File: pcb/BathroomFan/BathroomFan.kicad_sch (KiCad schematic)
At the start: 8 parts, among them U1 ESP32-DEVKIT-V1, U2 DHT11

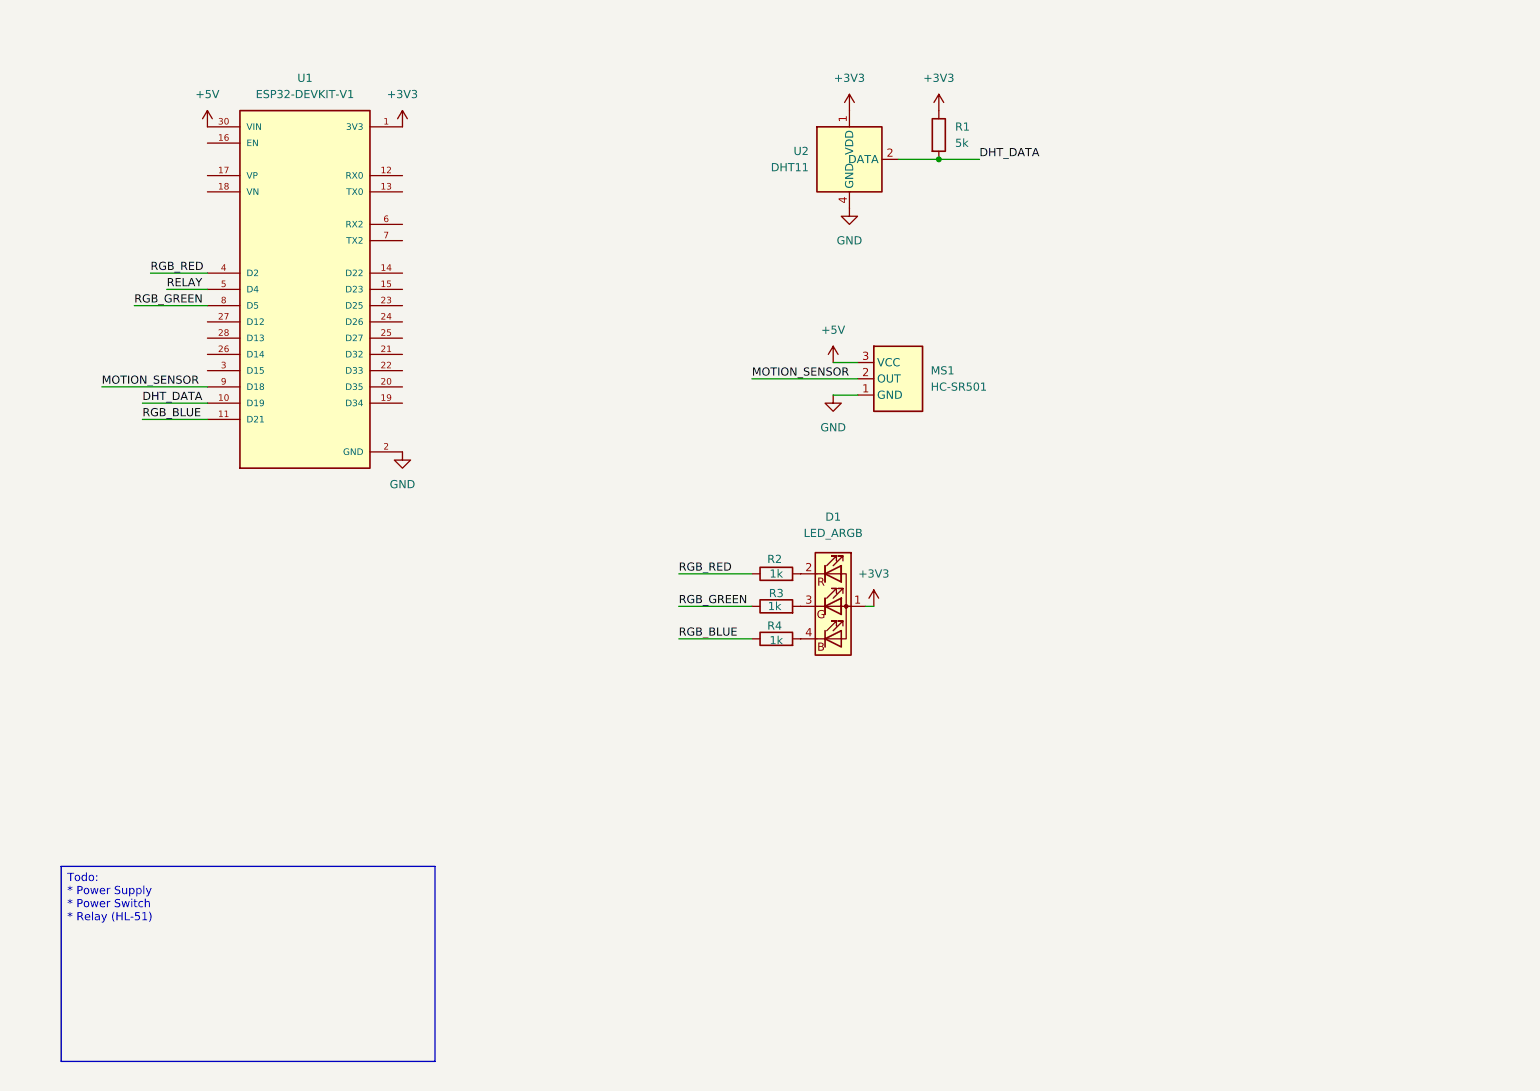
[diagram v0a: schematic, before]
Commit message: SCH - added ac/dc module with switch, relay and connectors for power and fan
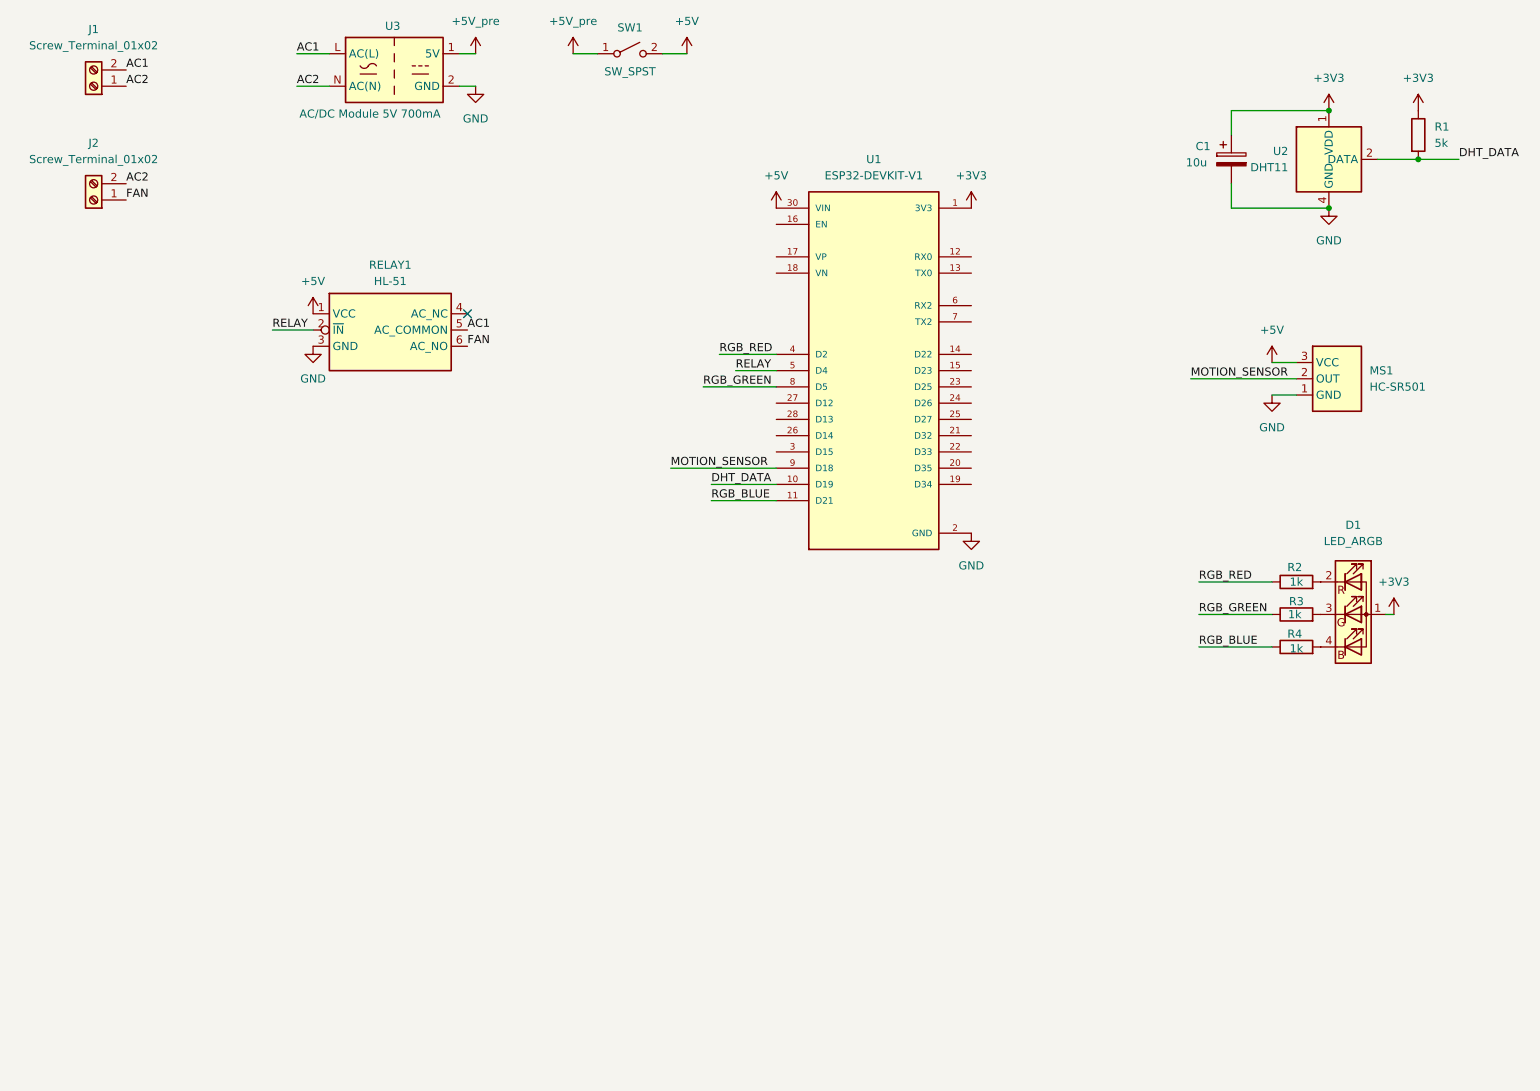
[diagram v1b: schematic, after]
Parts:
- added C1: 10u, symbol Device:C_Polarized
- added J1, J2: Screw_Terminal_01x02, symbol Connector:Screw_Terminal_01x02
- added RELAY1: HL-51, bathroom_fan:HL-51, symbol bathroom_fan:HL-51
- added SW1: SW_SPST, symbol Switch:SW_SPST
- added U3: AC/DC Module 5V 700mA, symbol bathroom_fan:AC-DC Module 5Vdc 700mA 85-265Vac
- D1: footprint (none) -> Connector_PinHeader_1.00mm:PinHeader_1x04_P1.00mm_Vertical
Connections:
- net +3V3: now also C1.1
- net +5V: now also RELAY1.1 (VCC), SW1.2 (B)
- net GND: now also C1.2, RELAY1.3 (GND), U3.2 (GND)
- net RELAY: now also RELAY1.2 (~{IN})
- new net +5V_pre: SW1.1 (A), U3.1 (5V)
- new net AC1: J1.2 (Pin_2), RELAY1.5 (AC_COMMON), U3.L (AC(L))
- new net AC2: J1.1 (Pin_1), J2.2 (Pin_2), U3.N (AC(N))
- new net FAN: J2.1 (Pin_1), RELAY1.6 (AC_NO)
- no-connect marks 0 -> 1
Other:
- moved on the sheet: D1, MS1, R1, R2, R3, R4, U1, U2

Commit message: improved relay footprint with actual part, added munting holes for screws
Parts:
- added H1, H2: MountingScrew, MountingHole:MountingHole_4.3mm_M4, symbol Auxiliary_Items:MountingScrew
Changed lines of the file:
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@@
+	)
+	(symbol
+		(lib_id "Auxiliary_Items:MountingScrew")
+		(at 137.16 179.07 0)
+		(unit 1)
+		(body_style 1)
+		(exclude_from_sim no)
+		(in_bom no)
+		(on_board yes)
+		(in_pos_files yes)
+		(dnp no)
+		(fields_autoplaced yes)
+		(property "Reference" "H2"
+			(at 137.16 175.006 0)
+			(hide yes)
+			(show_name no)
+			(do_not_autoplace no)
+			(effects
+				(font
+					(size 1.27 1.27)
+				)
+			)
+		)
+		(property "Value" "MountingScrew"
+			(at 137.16 182.626 0)
+			(hide yes)
+			(show_name no)
+			(do_not_autoplace no)
+			(effects
+				(font
+					(size 1.27 1.27)
+				)
+			)
+		)
+		(property "Footprint" "MountingHole:MountingHole_4.3mm_M4"
+			(at 137.16 179.07 0)
+			(hide yes)
+			(show_name no)
+			(do_not_autoplace no)
+			(effects
+				(font
+					(size 1.27 1.27)
+				)
+			)
+		)
+		(property "Datasheet" ""
+			(at 137.16 179.07 0)
+			(hide yes)
+			(show_name no)
+			(do_not_autoplace no)
+			(effects
+				(font
+					(size 1.27 1.27)
+				)
+			)
+		)
+		(property "Description" "Mounting screw"
+			(at 137.16 179.07 0)
+			(hide yes)
+			(show_name no)
+			(do_not_autoplace no)
+			(effects
+				(font
+					(size 1.27 1.27)
+				)
+			)
+		)
+		(instances
+			(project "BathroomFan"
+				(path "/4793d324-38ac-415b-8f0e-f54c1c7495b4"
+					(reference "H2")
+					(unit 1)
+				)
+			)
+		)
 	)
 	(symbol
@@
 					(unit 1)
 				)
+			)
+		)
+	)
+	(symbol
+		(lib_id "Auxiliary_Items:MountingScrew")
+		(at 132.08 179.07 0)
+		(unit 1)
+		(body_style 1)
+		(exclude_from_sim no)
+		(in_bom no)
+		(on_board yes)
+		(in_pos_files yes)
+		(dnp no)
+		(fields_autoplaced yes)
+		(property "Reference" "H1"
+			(at 132.08 175.006 0)
+			(hide yes)
+			(show_name no)
+			(do_not_autoplace no)
+			(effects
+				(font
+					(size 1.27 1.27)
+				)
+			)
+		)
+		(property "Value" "MountingScrew"
+			(at 132.08 182.626 0)
+			(hide yes)
+			(show_name no)
+			(do_not_autoplace no)
+			(effects
+				(font
+					(size 1.27 1.27)
+				)
+			)
+		)
+		(property "Footprint" "MountingHole:MountingHole_4.3mm_M4"
+			(at 132.08 179.07 0)
+			(hide yes)
+			(show_name no)
+			(do_not_autoplace no)
+			(effects
+				(font
+					(size 1.27 1.27)
+				)
+			)
+		)
+		(property "Datasheet" ""
+			(at 132.08 179.07 0)
+			(hide yes)
+			(show_name no)
+			(do_not_autoplace no)
+			(effects
+				(font
+					(size 1.27 1.27)
+				)
+			)
+		)
+		(property "Description" "Mounting screw"
+			(at 132.08 179.07 0)
+			(hide yes)
+			(show_name no)
+			(do_not_autoplace no)
+			(effects
+				(font
+					(size 1.27 1.27)
+				)
+			)
+		)
+		(instances
+			(project "BathroomFan"
+				(path "/4793d324-38ac-415b-8f0e-f54c1c7495b4"
+					(reference "H1")
+					(unit 1)
+				)

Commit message: PCB: initial Board format and component placement
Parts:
- C1: footprint (none) -> Capacitor_THT:CP_Radial_D4.0mm_P2.00mm
- D1: footprint Connector_PinHeader_1.00mm:PinHeader_1x04_P1.00mm_Vertical -> Connector_PinHeader_2.54mm:PinHeader_1x04_P2.54mm_Vertical
- J1: footprint (none) -> TerminalBlock_Phoenix:TerminalBlock_Phoenix_MKDS-1,5-2-5.08_1x02_P5.08mm_Horizontal; Name (none) -> POWER
- J2: footprint (none) -> TerminalBlock_Phoenix:TerminalBlock_Phoenix_MKDS-1,5-2-5.08_1x02_P5.08mm_Horizontal; Name (none) -> FAN
- MS1: footprint bathroom_fan:HC-SR501 -> Connector_PinHeader_2.54mm:PinHeader_1x03_P2.54mm_Vertical
- R1, R2, R3, R4: footprint (none) -> Resistor_SMD:R_0805_2012Metric_Pad1.20x1.40mm_HandSolder
- SW1: footprint (none) -> Connector_PinHeader_2.54mm:PinHeader_1x02_P2.54mm_Vertical
- U2: footprint Sensor:Aosong_DHT11_5.5x12.0_P2.54mm -> Connector_PinHeader_2.54mm:PinHeader_1x04_P2.54mm_Vertical
- U3: footprint (none) -> bathroom_fan:ACDC_Module_5V_700mA
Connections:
- net AC1: now also U3.N (AC(N)); no longer U3.L (AC(L))
- net AC2: now also U3.L (AC(L)); no longer U3.N (AC(N))
- net GND: now also U3.3 (GND); no longer U3.2 (GND)

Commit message: SCH and PCB: redistributed ESP32 pins for better layout, first version of layout finished
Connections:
- net MOTION_SENSOR: now also U1.28 (D13); no longer U1.9 (D18)
- net RELAY: now also U1.26 (D14); no longer U1.5 (D4)
- net RGB_BLUE: now also U1.5 (D4); no longer U1.11 (D21)
- net RGB_GREEN: now also U1.4 (D2); no longer U1.8 (D5)
- net RGB_RED: now also U1.3 (D15); no longer U1.4 (D2)
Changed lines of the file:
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@@
-	(wire
-		(pts
-			(xy 123.19 83.82) (xy 134.62 83.82)
-		)
-		(stroke
-			(width 0)
-			(type default)
-		)
-	)
 	(wire
 		(pts
@@
 	(wire
 		(pts
+			(xy 124.46 81.28) (xy 134.62 81.28)
+		)
+		(stroke
+			(width 0)
+			(type default)
+		)
+	)
+	(wire
+		(pts
 			(xy 205.74 52.07) (xy 205.74 55.88)
 		)
@@
 	(wire
 		(pts
-			(xy 124.46 101.6) (xy 134.62 101.6)
-		)
-		(stroke
-			(width 0)
-			(type default)
-		)
-	)
-	(wire
-		(pts
-			(xy 128.27 81.28) (xy 134.62 81.28)
-		)
-		(stroke
-			(width 0)
-			(type default)
-		)
-	)
-	(wire
-		(pts
 			(xy 85.09 36.83) (xy 87.63 36.83)
 		)
@@
 	(wire
 		(pts
+			(xy 123.19 78.74) (xy 134.62 78.74)
+		)
+		(stroke
+			(width 0)
+			(type default)
+		)
+	)
+	(wire
+		(pts
 			(xy 205.74 44.45) (xy 205.74 40.64)
 		)
@@
 	(wire
 		(pts
+			(xy 128.27 91.44) (xy 134.62 91.44)
+		)
+		(stroke
+			(width 0)
+			(type default)
+		)
+	)
+	(wire
+		(pts
 			(xy 124.46 99.06) (xy 134.62 99.06)
 		)
@@
 	(wire
 		(pts
-			(xy 125.73 78.74) (xy 134.62 78.74)
+			(xy 118.11 88.9) (xy 134.62 88.9)
 		)
 		(stroke
@@
 	(wire
 		(pts
+			(xy 125.73 93.98) (xy 134.62 93.98)
+		)
+		(stroke
+			(width 0)
+			(type default)
+		)
+	)
+	(wire
+		(pts
 			(xy 205.74 40.64) (xy 220.98 40.64)
 		)
@@
 		)
 	)
-	(wire
-		(pts
-			(xy 118.11 96.52) (xy 134.62 96.52)
-		)
-		(stroke
-			(width 0)
-			(type default)
+	(label "MOTION_SENSOR"
+		(at 118.11 88.9 0)
+		(effects
+			(font
+				(size 1.27 1.27)
+			)
+			(justify left bottom)
 		)
 	)
@@
 		)
 	)
-	(label "RGB_BLUE"
-		(at 124.46 101.6 0)
-		(effects
-			(font
-				(size 1.27 1.27)
-			)
-			(justify left bottom)
-		)
-	)
 	(label "AC1"
 		(at 86.36 74.93 0)
@@
 	)
 	(label "RGB_GREEN"
-		(at 123.19 83.82 0)
+		(at 123.19 78.74 0)
+		(effects
+			(font
+				(size 1.27 1.27)
+			)
+			(justify left bottom)
+		)
+	)
+	(label "RGB_RED"
+		(at 125.73 93.98 0)
 		(effects
 			(font
@@
 		)
 	)
+	(label "RGB_BLUE"
+		(at 124.46 81.28 0)
+		(effects
+			(font
+				(size 1.27 1.27)
+			)
+			(justify left bottom)
+		)
+	)
+	(label "RELAY"
+		(at 128.27 91.44 0)
+		(effects
+			(font
+				(size 1.27 1.27)
+			)
+			(justify left bottom)
+		)
+	)
 	(label "FAN"
 		(at 33.02 54.61 0)
@@
 	)
 	(label "RGB_RED"
-		(at 125.73 78.74 0)
-		(effects
-			(font
-				(size 1.27 1.27)
-			)
-			(justify left bottom)
-		)
-	)
-	(label "RGB_RED"
 		(at 200.66 114.3 0)
 		(effects
@@
 		)
 	)
-	(label "RELAY"
-		(at 128.27 81.28 0)
-		(effects
-			(font
-				(size 1.27 1.27)
-			)
-			(justify left bottom)
-		)
-	)
 	(label "AC1"
 		(at 33.02 34.29 0)
@@
 		(effects
 			(font
-				(size 1.27 1.27)
-			)
-			(justify left bottom)
-		)
-	)
-	(label "MOTION_SENSOR"
-		(at 118.11 96.52 0)
-		(effects
-			(font

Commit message: SCH and PCB: added logo, adjusted silk identifier
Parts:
- added G1: LOGO, bathroom_fan:LOGO, symbol bathroom_fan:LOGO
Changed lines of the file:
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@@
 	(title_block
 		(title "Bathroom Fan Controller")
-		(date "2026-07-05")
+		(date "2026-08-02")
 		(rev "1.0")
 		(company "brunolalb@gmail.com")
@@
 					(unit 1)
 				)
+			)
+		)
+	)
+	(symbol
+		(lib_id "bathroom_fan:LOGO")
+		(at 134.62 187.96 0)
+		(unit 1)
+		(body_style 1)
+		(exclude_from_sim no)
+		(in_bom no)
+		(on_board yes)
+		(in_pos_files yes)
+		(dnp no)
+		(fields_autoplaced yes)
+		(property "Reference" "G1"
+			(at 134.62 183.5948 0)
+			(hide yes)
+			(show_name no)
+			(do_not_autoplace no)
+			(effects
+				(font
+					(size 1.27 1.27)
+				)
+			)
+		)
+		(property "Value" "LOGO"
+			(at 134.62 192.3252 0)
+			(hide yes)
+			(show_name no)
+			(do_not_autoplace no)
+			(effects
+				(font
+					(size 1.27 1.27)
+				)
+			)
+		)
+		(property "Footprint" "bathroom_fan:LOGO"
+			(at 134.874 194.056 0)
+			(hide yes)
+			(show_name no)
+			(do_not_autoplace no)
+			(effects
+				(font
+					(size 1.27 1.27)
+				)
+			)
+		)
+		(property "Datasheet" ""
+			(at 134.62 187.96 0)
+			(hide yes)
+			(show_name no)
+			(do_not_autoplace no)
+			(effects
+				(font
+					(size 1.27 1.27)
+				)
+			)
+		)
+		(property "Description" ""
+			(at 134.62 187.96 0)
+			(hide yes)
+			(show_name no)
+			(do_not_autoplace no)
+			(effects
+				(font
+					(size 1.27 1.27)
+				)
+			)
+		)
+		(instances
+			(project "BathroomFan"
+				(path "/4793d324-38ac-415b-8f0e-f54c1c7495b4"
+					(reference "G1")
+					(unit 1)
+				)
